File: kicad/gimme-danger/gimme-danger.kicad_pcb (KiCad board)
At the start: 4 copper layers, 48 x 42 mm, 94 parts, among them J3 Screw_Terminal_01x06, Q1 AO3400A, Q2 AO3400A, Q3 AO3400A, Q4 AO3400A, U1 ESP32-S3-WROOM-1, U11 DDTC143EUA, U2 TYPE-C-31-M-12, U3 TPD4E1U06DCKR, U4 DC-84, U5 SKRKAEE020, U7 SKRKAEE020, U8 TPS54302, U9 INA219AIDR

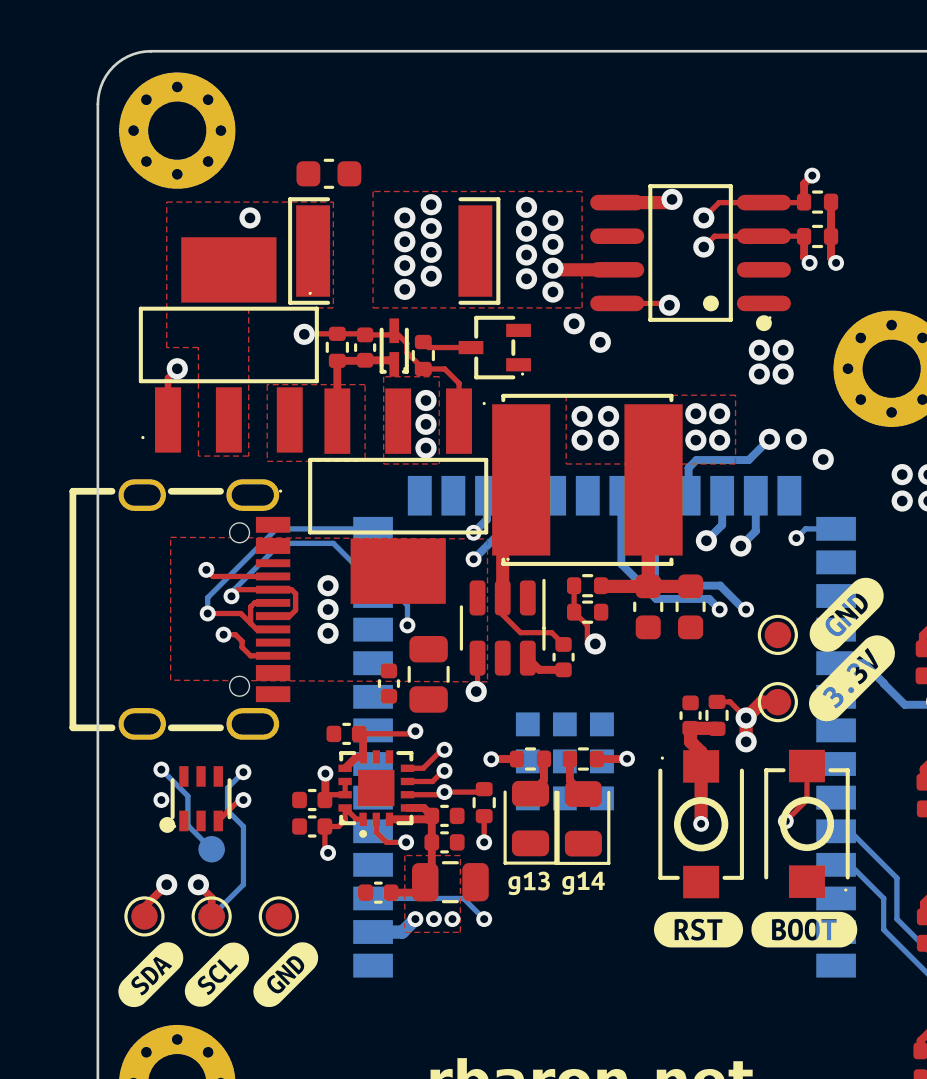
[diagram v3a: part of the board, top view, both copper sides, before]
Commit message: No more DRC errors -- only 78 warnings
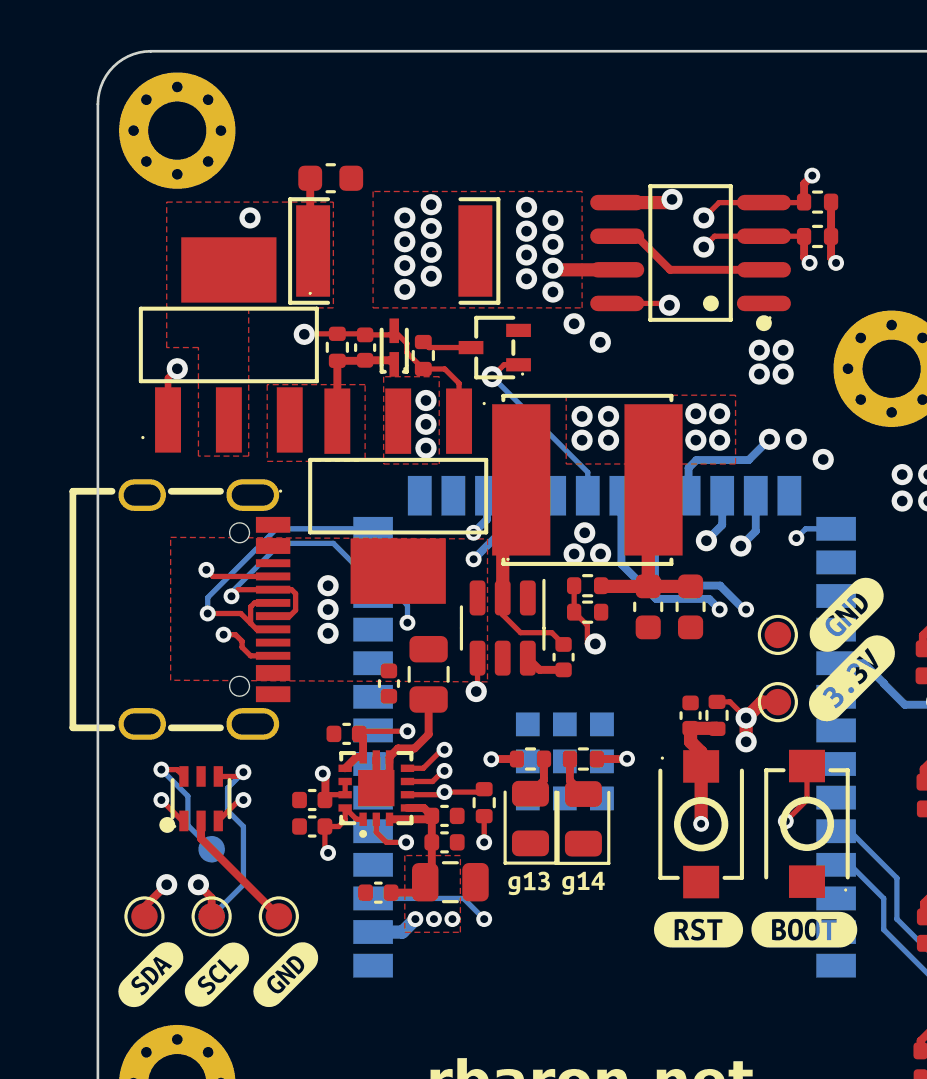
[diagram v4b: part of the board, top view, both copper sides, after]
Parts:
- moved C1 0.18 mm to (68.0, 95.7)
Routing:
- net GND: track 0.00 -> 16.6 mm, vias 8 -> 11
- net LOAD_EN#: track 0.00 -> 7.18 mm, vias 0 -> 1
- net VSh+: track 21.4 -> 24.2 mm
- net D-: track 20.2 -> 21.4 mm
- net CC2: track 22.8 -> 23.8 mm
- net CC1: track 28.8 -> 29.4 mm
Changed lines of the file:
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@@
   )
   (footprint "Capacitor_SMD:C_0603_1608Metric" (layer "F.Cu")
-    (at 67.932 95.533)
+    (at 68 95.7)
     (descr "Capacitor SMD 0603 (1608 Metric), square (rectangular) end terminal, IPC_7351 nominal, (Body size source: IPC-SM-782 page 76, https://www.pcb-3d.com/wordpress/wp-content/uploads/ipc-sm-782a_amendment_1_and_2.pdf), generated with kicad-footprint-generator")
     (tags "capacitor")
@@
     )
   )
+  (segment (start 67.225 98.341294) (end 67.333706 98.45) (width 0.3) (layer "F.Cu") (net 1))
   (segment (start 80.730398 100.430398) (end 80.8 100.5) (width 0.2) (layer "F.Cu") (net 1))
   (segment (start 78.827584 100.430398) (end 80.730398 100.430398) (width 0.2) (layer "F.Cu") (net 1))
+  (segment (start 67.225 95.7) (end 67.225 98.341294) (width 0.3) (layer "F.Cu") (net 1))
   (via (at 64.95 97.2) (size 0.8) (drill 0.4) (layers "F.Cu" "B.Cu") (net 1))
   (via (at 80.8 100.5) (size 0.8) (drill 0.4) (layers "F.Cu" "B.Cu") (net 1))
@@
   (segment (start 84.065 109.035) (end 84.065 107.7) (width 0.3) (layer "B.Cu") (net 14))
   (segment (start 83.5 109.6) (end 84.065 109.035) (width 0.3) (layer "B.Cu") (net 14))
+  (segment (start 78.827584 97.890393) (end 79.556083 97.890393) (width 0.3) (layer "F.Cu") (net 25))
+  (segment (start 70.222581 117.572518) (end 70.222581 118.249937) (width 0.3) (layer "F.Cu") (net 25))
+  (segment (start 71.7 116.719239) (end 71.7 115.4) (width 0.3) (layer "F.Cu") (net 25))
+  (segment (start 63.1 119.98998) (end 63.1 120.66) (width 0.3) (layer "F.Cu") (net 25))
+  (segment (start 69.722454 117.572518) (end 69.722454 118.750064) (width 0.3) (layer "F.Cu") (net 25))
+  (segment (start 70.222581 118.249937) (end 69.722454 118.750064) (width 0.3) (layer "F.Cu") (net 25))
+  (segment (start 79.556083 97.890393) (end 80.826085 99.160395) (width 0.3) (layer "F.Cu") (net 25))
+  (segment (start 63.1 120.66) (end 66.04 123.6) (width 0.3) (layer "F.Cu") (net 25))
+  (segment (start 80.826085 99.160395) (end 84.372416 99.160395) (width 0.3) (layer "F.Cu") (net 25))
+  (segment (start 71.169239 117.25) (end 71.7 116.719239) (width 0.3) (layer "F.Cu") (net 25))
+  (segment (start 70.222581 117.572518) (end 70.545099 117.25) (width 0.3) (layer "F.Cu") (net 25))
+  (segment (start 70.545099 117.25) (end 71.169239 117.25) (width 0.3) (layer "F.Cu") (net 25))
   (via (at 85.1 102.2) (size 0.8) (drill 0.4) (layers "F.Cu" "B.Cu") (free) (net 25))
   (via (at 90.6 106.9) (size 0.8) (drill 0.4) (layers "F.Cu" "B.Cu") (free) (net 25))
+  (via (at 78.2 109.9) (size 0.8) (drill 0.4) (layers "F.Cu" "B.Cu") (free) (net 25))
   (via (at 89.6 106.9) (size 0.8) (drill 0.4) (layers "F.Cu" "B.Cu") (free) (net 25))
   (via (at 84.2 103.1) (size 0.8) (drill 0.4) (layers "F.Cu" "B.Cu") (free) (net 25))
+  (via (at 77.6 109.1) (size 0.8) (drill 0.4) (layers "F.Cu" "B.Cu") (free) (net 25))
   (via (at 85.1 103.1) (size 0.8) (drill 0.4) (layers "F.Cu" "B.Cu") (free) (net 25))
   (via (at 89.6 107.9) (size 0.8) (drill 0.4) (layers "F.Cu" "B.Cu") (free) (net 25))
   (via (at 84.2 102.2) (size 0.8) (drill 0.4) (layers "F.Cu" "B.Cu") (free) (net 25))
   (via (at 90.6 107.9) (size 0.8) (drill 0.4) (layers "F.Cu" "B.Cu") (free) (net 25))
+  (via (at 77.2 109.9) (size 0.8) (drill 0.4) (layers "F.Cu" "B.Cu") (free) (net 25))
   (segment (start 86.91 96.6) (end 86.91 97.9) (width 0.3) (layer "F.Cu") (net 26))
   (segment (start 84.9 115.5) (end 84.3 115.5) (width 0.5) (layer "F.Cu") (net 26))
@@
   (via (at 83.7 116.1) (size 0.8) (drill 0.4) (layers "F.Cu" "B.Cu") (net 26))
   (via (at 78.5 105.6) (size 0.8) (drill 0.4) (layers "F.Cu" "B.Cu") (free) (net 26))
-  (via (at 67.8 118.2) (size 0.6) (drill 0.3) (layers "F.Cu" "B.Cu") (net 26))
+  (via (at 67.7 118.2) (size 0.6) (drill 0.3) (layers "F.Cu" "B.Cu") (net 26))
   (via (at 78.5 104.7) (size 0.8) (drill 0.4) (layers "F.Cu" "B.Cu") (free) (net 26))
   (segment (start 70.71 124.19) (end 69.6 124.19) (width 0.5) (layer "B.Cu") (net 26))
@@
   (segment (start 73.02 122.92) (end 73.8 123.7) (width 0.2) (layer "B.Cu") (net 28))
   (segment (start 69.6 122.92) (end 73.02 122.92) (width 0.2) (layer "B.Cu") (net 28))
-  (segment (start 69.08 116.7) (end 71.1 116.7) (width 0.2) (layer "F.Cu") (net 29))
   (segment (start 65.8226 110.750064) (end 64.450064 110.750064) (width 0.2) (layer "F.Cu") (net 29))
-  (segment (start 71.1 116.7) (end 71.2 116.6) (width 0.3) (layer "F.Cu") (net 29))
+  (segment (start 69.18 116.6) (end 69.08 116.7) (width 0.2) (layer "F.Cu") (net 29))
+  (segment (start 70.9 116.6) (end 69.18 116.6) (width 0.2) (layer "F.Cu") (net 29))
   (segment (start 63.550064 110.750064) (end 63.3 110.5) (width 0.2) (layer "F.Cu") (net 29))
   (segment (start 68.544908 118) (end 68.97239 117.572518) (width 0.3) (layer "F.Cu") (net 29))
+  (segment (start 62.189993 118.05) (end 62.450013 118.31002) (width 0.2) (layer "F.Cu") (net 29))
   (segment (start 69.222581 117.572518) (end 69.222581 116.842581) (width 0.3) (layer "F.Cu") (net 29))
   (segment (start 69.222581 116.842581) (end 69.08 116.7) (width 0.3) (layer "F.Cu") (net 29))
   (segment (start 68.97239 117.572518) (end 69.222581 117.572518) (width 0.3) (layer "F.Cu") (net 29))
   (segment (start 64.450064 110.750064) (end 63.550064 110.750064) (width 0.2) (layer "F.Cu") (net 29))
+  (segment (start 61.6 118.05) (end 62.189993 118.05) (width 0.2) (layer "F.Cu") (net 29))
   (via (at 61.6 118.05) (size 0.6) (drill 0.3) (layers "F.Cu" "B.Cu") (net 29))
   (via (at 63.3 110.5) (size 0.6) (drill 0.3) (layers "F.Cu" "B.Cu") (net 29))
-  (via (at 71.2 116.6) (size 0.6) (drill 0.3) (layers "F.Cu" "B.Cu") (net 29))
+  (via (at 70.9 116.6) (size 0.6) (drill 0.3) (layers "F.Cu" "B.Cu") (net 29))
+  (segment (start 70.4 117.4) (end 70.9 116.9) (width 0.2) (layer "In1.Cu") (net 29))
   (segment (start 62.25 117.4) (end 70.4 117.4) (width 0.2) (layer "In1.Cu") (net 29))
   (segment (start 61.6 118.05) (end 62.25 117.4) (width 0.2) (layer "In1.Cu") (net 29))
-  (segment (start 70.4 117.4) (end 71.2 116.6) (width 0.2) (layer "In1.Cu") (net 29))
+  (segment (start 70.9 116.9) (end 70.9 116.6) (width 0.2) (layer "In1.Cu") (net 29))
   (segment (start 61.97434 111.82566) (end 61.97434 117.67566) (width 0.2) (layer "In2.Cu") (net 29))
   (segment (start 61.97434 117.67566) (end 61.6 118.05) (width 0.2) (layer "In2.Cu") (net 29))
@@
   (via (at 82.1 98.3) (size 0.8) (drill 0.4) (layers "F.Cu" "B.Cu") (net 34))
   (via (at 72.3 117.300497) (size 0.6) (drill 0.3) (layers "F.Cu" "B.Cu") (net 34))
-  (via (at 70.9 112.6) (size 0.6) (drill 0.3) (layers "F.Cu" "B.Cu") (net 34))
+  (via (at 70.9 112.5) (size 0.6) (drill 0.3) (layers "F.Cu" "B.Cu") (net 34))
   (via (at 61.8 122.4) (size 0.8) (drill 0.4) (layers "F.Cu" "B.Cu") (net 34))
   (via (at 86.1 98.9) (size 0.6) (drill 0.3) (layers "F.Cu" "B.Cu") (net 34))
@@
   (segment (start 65.951471 108.95) (end 69.6 108.95) (width 0.2) (layer "B.Cu") (net 45))
   (segment (start 65.8226 111.249936) (end 64.500064 111.249936) (width 0.2) (layer "F.Cu") (net 46))
+  (segment (start 62.450013 119.98998) (end 62.38998 119.98998) (width 0.2) (layer "F.Cu") (net 46))
   (segment (start 66.6726 111.400064) (end 66.6726 112.0274) (width 0.2) (layer "F.Cu") (net 46))
   (segment (start 66.522472 111.249936) (end 66.6726 111.400064) (width 0.2) (layer "F.Cu") (net 46))
+  (segment (start 62.38998 119.98998) (end 61.6 119.2) (width 0.2) (layer "F.Cu") (net 46))
   (segment (start 65.8226 111.249936) (end 66.522472 111.249936) (width 0.2) (layer "F.Cu") (net 46))
   (segment (start 64.500064 111.249936) (end 64.25 111.5) (width 0.2) (layer "F.Cu") (net 46))
@@
   (segment (start 75.8925 114.28) (end 75.45 113.8375) (width 0.3) (layer "F.Cu") (net 47))
   (segment (start 76.8 114.28) (end 75.8925 114.28) (width 0.3) (layer "F.Cu") (net 47))
+  (segment (start 74.550013 102.749987) (end 74.1 103.2) (width 0.2) (layer "F.Cu") (net 48))
+  (segment (start 75.097892 102.749987) (end 74.550013 102.749987) (width 0.2) (layer "F.Cu") (net 48))
+  (via (at 74.1 103.2) (size 0.8) (drill 0.4) (layers "F.Cu" "B.Cu") (net 48))
+  (segment (start 74.1 103.2) (end 77.715 106.815) (width 0.2) (layer "B.Cu") (net 48))
+  (segment (start 77.715 106.815) (end 77.715 107.7) (width 0.2) (layer "B.Cu") (net 48))
   (segment (start 75.1 107.1) (end 74.5 107.7) (width 0.5) (layer "F.Cu") (net 49))
   (segment (start 76.355 112.875) (end 75.175 112.875) (width 0.2) (layer "F.Cu") (net 49))
@@
   (segment (start 67.78 121.08) (end 67.9 121.2) (width 0.2) (layer "F.Cu") (net 55))
   (segment (start 68.3 120.2) (end 68.544908 119.955092) (width 0.2) (layer "F.Cu") (net 55))
+  (segment (start 63.749987 118.31002) (end 64.53998 118.31002) (width 0.2) (layer "F.Cu") (net 55))
   (segment (start 64.9726 113.750064) (end 64.65 113.427464) (width 0.2) (layer "F.Cu") (net 55))
+  (segment (start 64.53998 118.31002) (end 64.7 118.15) (width 0.2) (layer "F.Cu") (net 55))
   (segment (start 64.65 113.2) (end 64.4 112.95) (width 0.2) (layer "F.Cu") (net 55))
   (segment (start 67.78 120.2) (end 68.3 120.2) (width 0.2) (layer "F.Cu") (net 55))

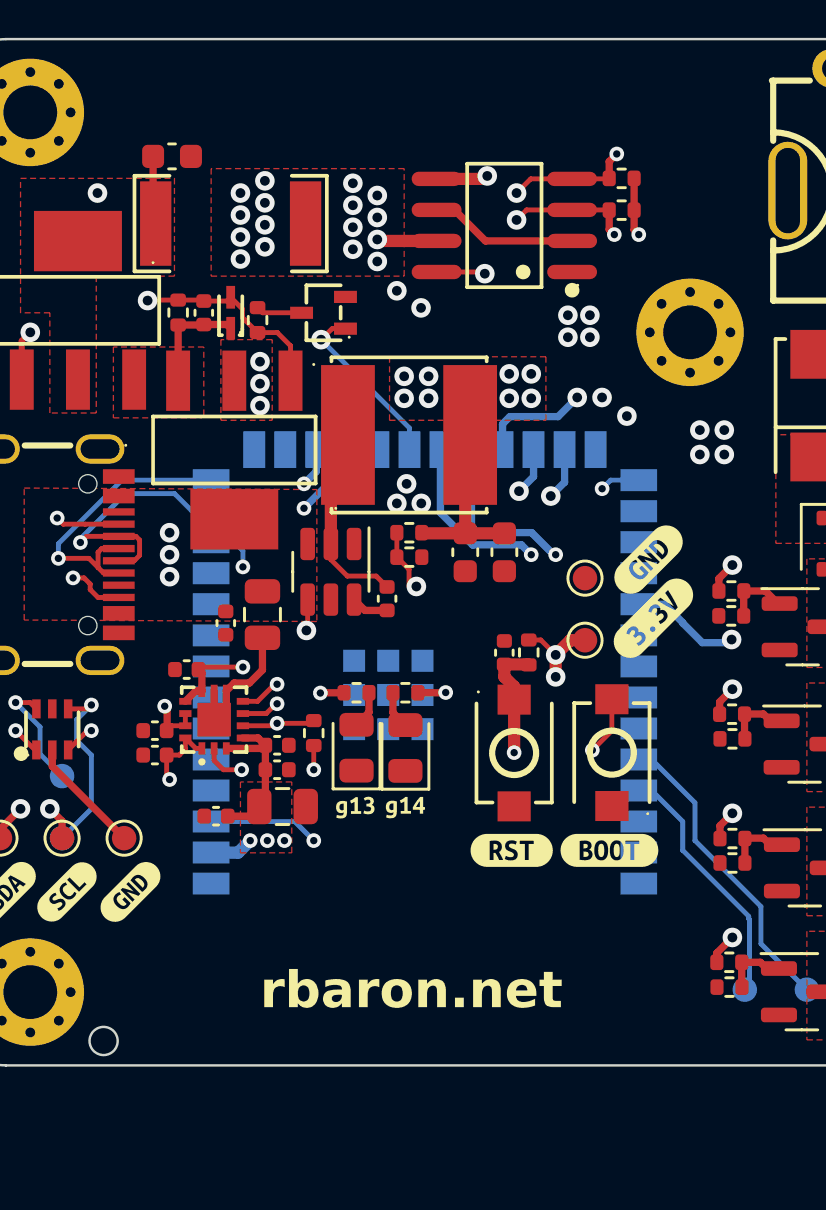
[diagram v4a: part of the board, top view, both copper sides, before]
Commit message: Routing 0.0.2a v1
No DCR errors
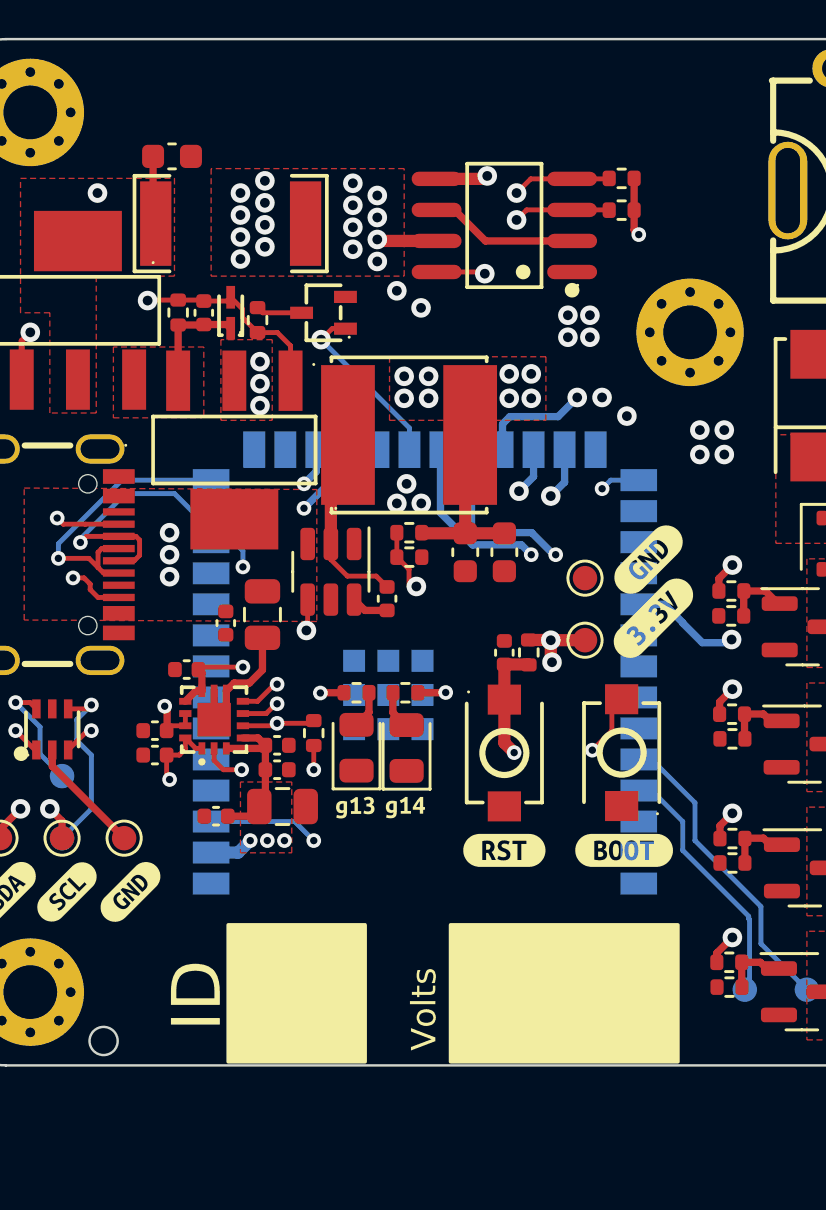
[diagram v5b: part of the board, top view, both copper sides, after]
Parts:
- removed kibuzzard-660041C0: G***, kibuzzard-660041C0
- removed kibuzzard-660041C6: G***, kibuzzard-660041C6
- removed kibuzzard-660041D1: G***, kibuzzard-660041D1
- removed kibuzzard-66004888: G***, kibuzzard-66004888
- added kibuzzard-660051B9: G***, kibuzzard-660051B9, B.Cu at (91.4, 131.7)
- added kibuzzard-660051C1: G***, kibuzzard-660051C1, B.Cu at (94.0, 131.7)
- added kibuzzard-660051C8: G***, kibuzzard-660051C8, B.Cu at (96.5, 131.7)
- added kibuzzard-66005479: G***, kibuzzard-66005479, B.Cu at (78.5, 93.5)
- moved kibuzzard-660044E7 0.60 mm to (86.5, 124.1)
- moved U5 0.40 mm to (81.6, 120.1)
- moved U7 0.40 mm to (86.4, 120.1)
- moved kibuzzard-660044E2 0.30 mm to (81.6, 124.1)
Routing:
- net +3V3: track 29.2 -> 27.2 mm
- net SCL: track 50.4 -> 49.3 mm, vias 6 -> 5
- net SDA: track 49.8 -> 48.8 mm, vias 6 -> 5
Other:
- board text added: "ID"
- board text added: "Volts"
- board text removed: "rbaron.net"
